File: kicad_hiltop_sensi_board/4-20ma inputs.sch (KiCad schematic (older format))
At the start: 44 parts, among them U12 MAX4194, U16 MAX4194, U19 MAX4194, U20 MAX4194

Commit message: revb design updated schematics and layout
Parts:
- R13, R49, R53, R55, R63, R64, R65, R67: value 10R -> 68R; Tolerance (none) -> 0.1%
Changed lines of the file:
@@
-$EndComp
-$Comp
-L device:R R13
-U 1 1 5DE1E542
-P 2400 2050
-F 0 "R13" V 2193 2050 50  0000 C CNN
-F 1 "10R" V 2284 2050 50  0000 C CNN
-F 2 "Resistor_SMD:R_0603_1608Metric" V 2330 2050 50  0001 C CNN
-F 3 "" H 2400 2050 50  0001 C CNN
-F 4 "101-058" H 2400 2050 50  0001 C CNN "Devtank"
-	1    2400 2050
-	0    1    1    0
 $EndComp
 $Comp
@@
 P 2400 2450
 F 0 "R49" V 2193 2450 50  0000 C CNN
-F 1 "10R" V 2284 2450 50  0000 C CNN
+F 1 "68R" V 2284 2450 50  0000 C CNN
 F 2 "Resistor_SMD:R_0603_1608Metric" V 2330 2450 50  0001 C CNN
 F 3 "" H 2400 2450 50  0001 C CNN
 F 4 "101-058" H 2400 2450 50  0001 C CNN "Devtank"
+F 5 "0.1%" V 2400 2450 50  0000 C CNN "Tolerance"
 	1    2400 2450
 	0    1    1    0
@@
 P 6590 2045
 F 0 "R65" V 6383 2045 50  0000 C CNN
-F 1 "10R" V 6474 2045 50  0000 C CNN
+F 1 "68R" V 6474 2045 50  0000 C CNN
 F 2 "Resistor_SMD:R_0603_1608Metric" V 6520 2045 50  0001 C CNN
 F 3 "" H 6590 2045 50  0001 C CNN
 F 4 "101-058" H 6590 2045 50  0001 C CNN "Devtank"
+F 5 "0.1%" V 6590 2045 50  0000 C CNN "Tolerance"
 	1    6590 2045
 	0    1    1    0
@@
 P 6590 2445
 F 0 "R67" V 6383 2445 50  0000 C CNN
-F 1 "10R" V 6474 2445 50  0000 C CNN
+F 1 "68R" V 6474 2445 50  0000 C CNN
 F 2 "Resistor_SMD:R_0603_1608Metric" V 6520 2445 50  0001 C CNN
 F 3 "" H 6590 2445 50  0001 C CNN
 F 4 "101-058" H 6590 2445 50  0001 C CNN "Devtank"
+F 5 "0.1%" V 6590 2445 50  0000 C CNN "Tolerance"
 	1    6590 2445
 	0    1    1    0
@@
 P 2400 4250
 F 0 "R53" V 2193 4250 50  0000 C CNN
-F 1 "10R" V 2284 4250 50  0000 C CNN
+F 1 "68R" V 2284 4250 50  0000 C CNN
 F 2 "Resistor_SMD:R_0603_1608Metric" V 2330 4250 50  0001 C CNN
 F 3 "" H 2400 4250 50  0001 C CNN
 F 4 "101-058" H 2400 4250 50  0001 C CNN "Devtank"
+F 5 "0.1%" V 2400 4250 50  0000 C CNN "Tolerance"
 	1    2400 4250
 	0    1    1    0
@@
 P 2400 4650
 F 0 "R55" V 2193 4650 50  0000 C CNN
-F 1 "10R" V 2284 4650 50  0000 C CNN
+F 1 "68R" V 2284 4650 50  0000 C CNN
 F 2 "Resistor_SMD:R_0603_1608Metric" V 2330 4650 50  0001 C CNN
 F 3 "" H 2400 4650 50  0001 C CNN
 F 4 "101-058" H 2400 4650 50  0001 C CNN "Devtank"
+F 5 "0.1%" V 2400 4650 50  0000 C CNN "Tolerance"
 	1    2400 4650
 	0    1    1    0
@@
 P 6505 4250
 F 0 "R63" V 6298 4250 50  0000 C CNN
-F 1 "10R" V 6389 4250 50  0000 C CNN
+F 1 "68R" V 6389 4250 50  0000 C CNN
 F 2 "Resistor_SMD:R_0603_1608Metric" V 6435 4250 50  0001 C CNN
 F 3 "" H 6505 4250 50  0001 C CNN
 F 4 "101-058" H 6505 4250 50  0001 C CNN "Devtank"
+F 5 "0.1%" V 6505 4250 50  0000 C CNN "Tolerance"
 	1    6505 4250
 	0    1    1    0
@@
 P 6505 4650
 F 0 "R64" V 6298 4650 50  0000 C CNN
-F 1 "10R" V 6389 4650 50  0000 C CNN
+F 1 "68R" V 6389 4650 50  0000 C CNN
 F 2 "Resistor_SMD:R_0603_1608Metric" V 6435 4650 50  0001 C CNN
 F 3 "" H 6505 4650 50  0001 C CNN
 F 4 "101-058" H 6505 4650 50  0001 C CNN "Devtank"
+F 5 "0.1%" V 6505 4650 50  0000 C CNN "Tolerance"
 	1    6505 4650
 	0    1    1    0
@@
 Text Notes 3600 5955 0    60   ~ 0
 Updated calculation for sense resistor 30R. Replace 12.5K resistor with 11.5K.
+$Comp
+L device:R R13
+U 1 1 5DE1E542
+P 2400 2050
+F 0 "R13" V 2193 2050 50  0000 C CNN
+F 1 "68R" V 2284 2050 50  0000 C CNN
+F 2 "Resistor_SMD:R_0603_1608Metric" V 2330 2050 50  0001 C CNN
+F 3 "" H 2400 2050 50  0001 C CNN
+F 4 "101-058" H 2400 2050 50  0001 C CNN "Devtank"
+F 5 "0.1%" V 2400 2050 50  0000 C CNN "Tolerance"
+	1    2400 2050
+	0    1    1    0
+$EndComp
 $EndSCHEMATC

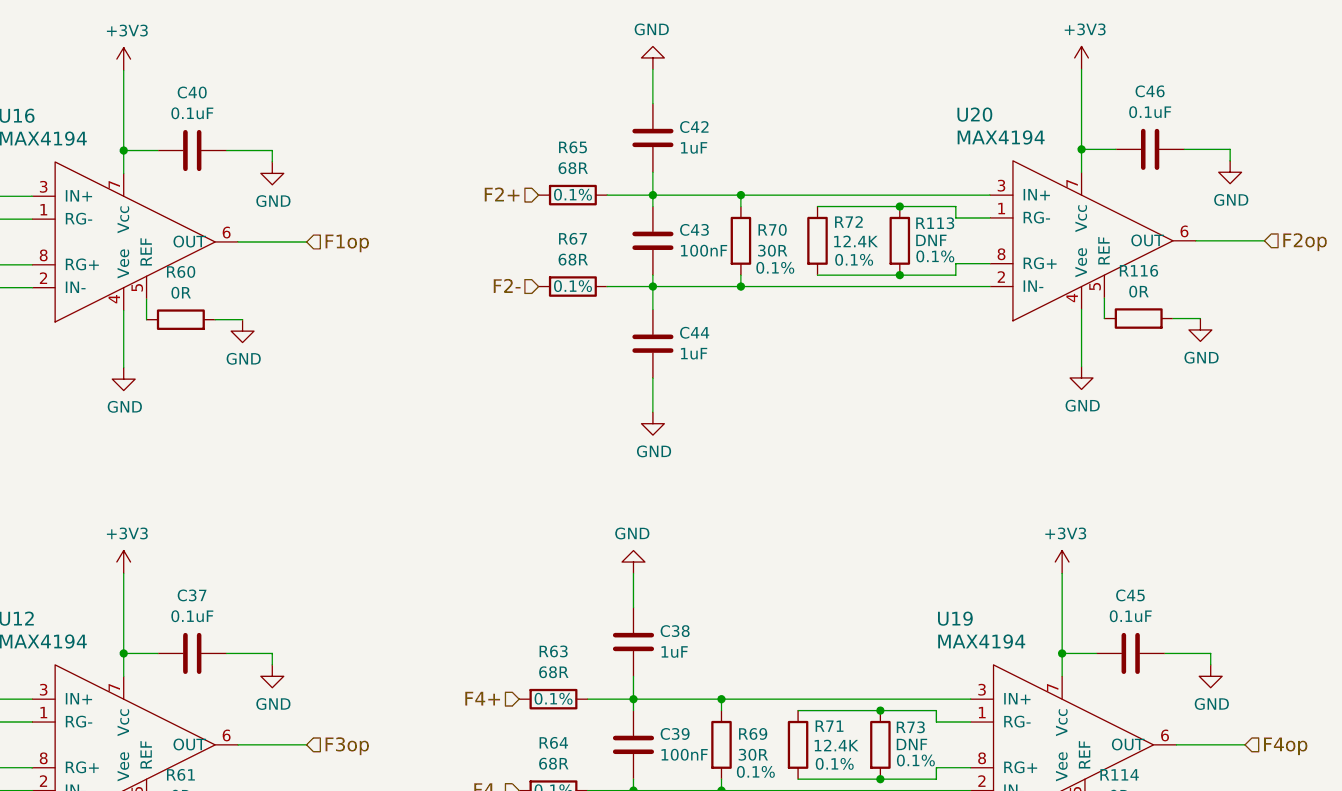
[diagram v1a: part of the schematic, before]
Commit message: updated footprints to simplify bom
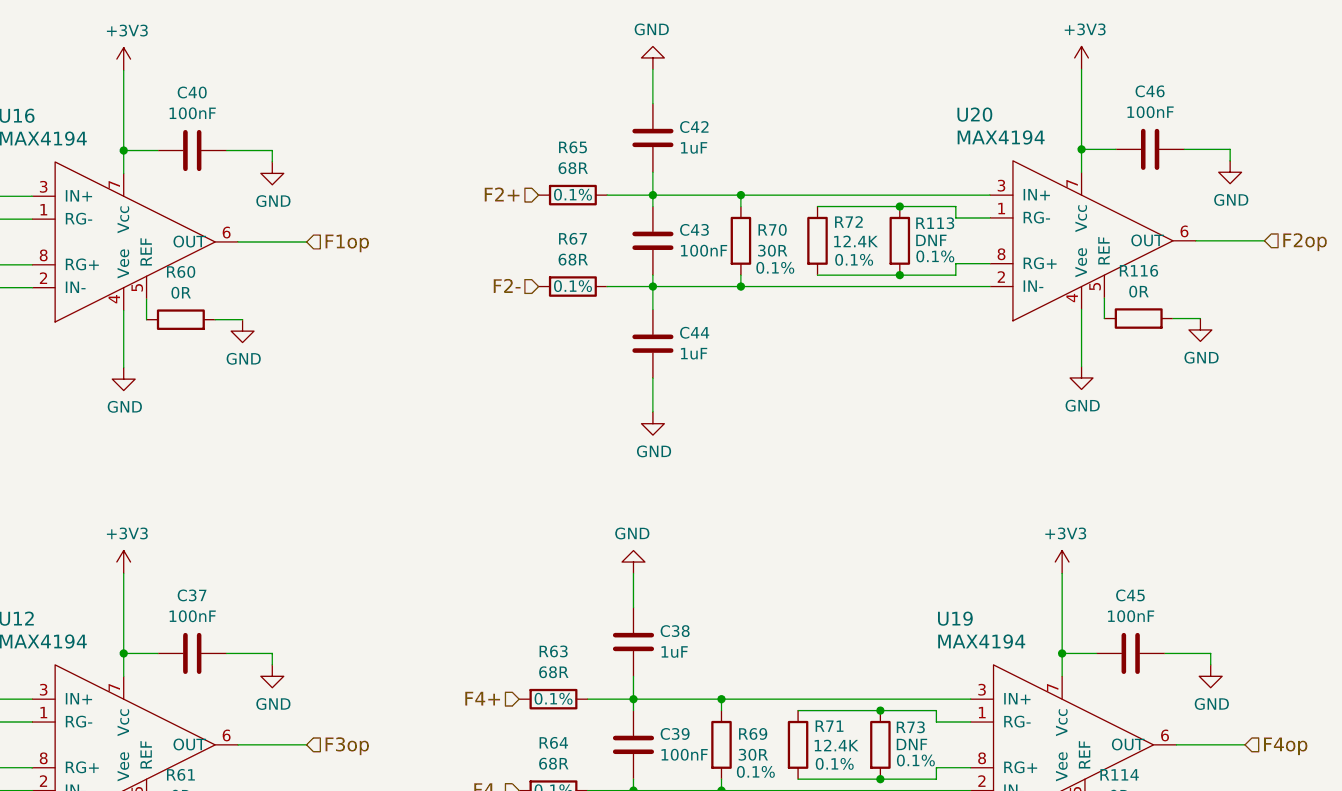
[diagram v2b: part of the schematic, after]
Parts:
- C37, C40, C45, C46: value 0.1uF -> 100nF
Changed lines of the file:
@@
 P 4925 1850
 F 0 "C40" V 4673 1850 50  0000 C CNN
-F 1 "0.1uF" V 4764 1850 50  0000 C CNN
+F 1 "100nF" V 4764 1850 50  0000 C CNN
 F 2 "Capacitor_SMD:C_0402_1005Metric" H 4963 1700 50  0001 C CNN
 F 3 "" H 4925 1850 50  0001 C CNN
@@
 P 9115 1845
 F 0 "C46" V 8863 1845 50  0000 C CNN
-F 1 "0.1uF" V 8954 1845 50  0000 C CNN
+F 1 "100nF" V 8954 1845 50  0000 C CNN
 F 2 "Capacitor_SMD:C_0402_1005Metric" H 9153 1695 50  0001 C CNN
 F 3 "" H 9115 1845 50  0001 C CNN
@@
 P 4925 4050
 F 0 "C37" V 4673 4050 50  0000 C CNN
-F 1 "0.1uF" V 4764 4050 50  0000 C CNN
+F 1 "100nF" V 4764 4050 50  0000 C CNN
 F 2 "Capacitor_SMD:C_0402_1005Metric" H 4963 3900 50  0001 C CNN
 F 3 "" H 4925 4050 50  0001 C CNN
@@
 P 9030 4050
 F 0 "C45" V 8778 4050 50  0000 C CNN
-F 1 "0.1uF" V 8869 4050 50  0000 C CNN
+F 1 "100nF" V 8869 4050 50  0000 C CNN
 F 2 "Capacitor_SMD:C_0402_1005Metric" H 9068 3900 50  0001 C CNN
 F 3 "" H 9030 4050 50  0001 C CNN
